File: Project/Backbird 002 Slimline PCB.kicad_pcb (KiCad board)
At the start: 2 copper layers, 14 x 116 mm, 10 parts

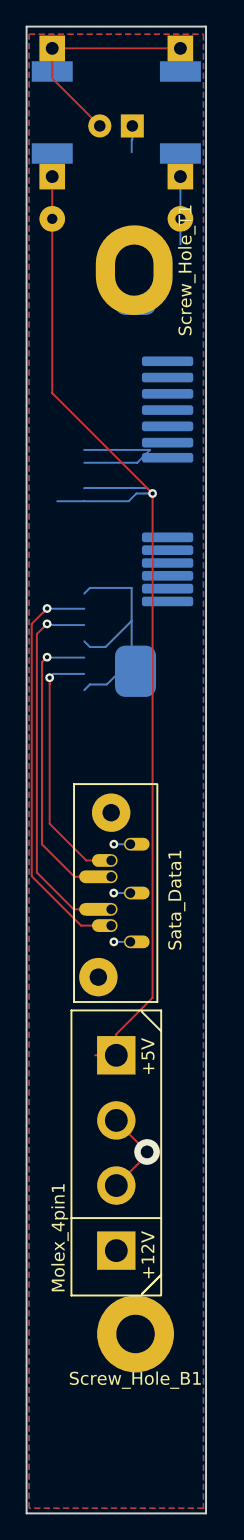
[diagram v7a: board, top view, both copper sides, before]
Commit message: Improved trace widths and zone fills
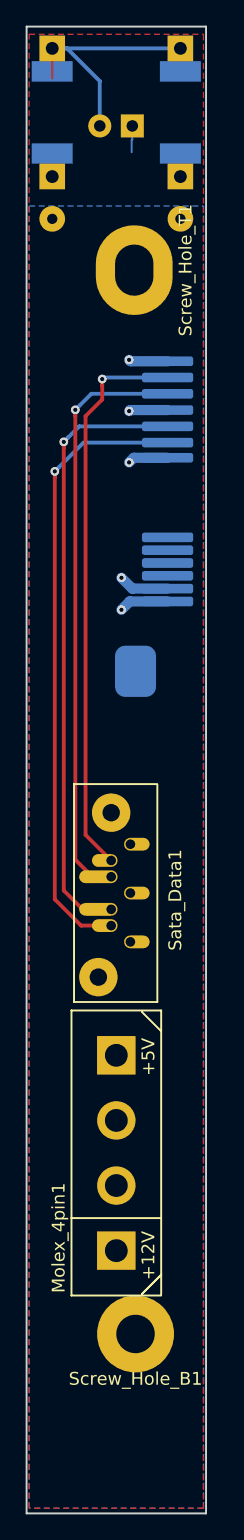
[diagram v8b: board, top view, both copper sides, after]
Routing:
- net +5V: track 87.8 -> 0.00 mm, vias 1 -> 0
- net A+: track 20.2 -> 44.1 mm
- net A-: track 24.1 -> 46.2 mm
- net (no net): track 18.9 -> 0.00 mm
- net B-: track 30.3 -> 48.6 mm
- net B+: track 32.1 -> 48.4 mm
- net GND: track 31.5 -> 21.7 mm, vias 4 -> 5
- net Net-(D1-Pad2): track 17.6 -> 20.6 mm
- added copper zone on B.Cu, net +5V
- added copper zone on F.Cu, net GND
- removed copper zone on F.Cu, net +5V
- removed copper zone on B.Cu, net GND
